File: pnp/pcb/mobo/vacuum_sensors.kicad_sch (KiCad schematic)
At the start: 18 parts, among them J33 I2C_AUX, U2 XGZP6857D, U3 XGZP6857D, U4 PCA9545A

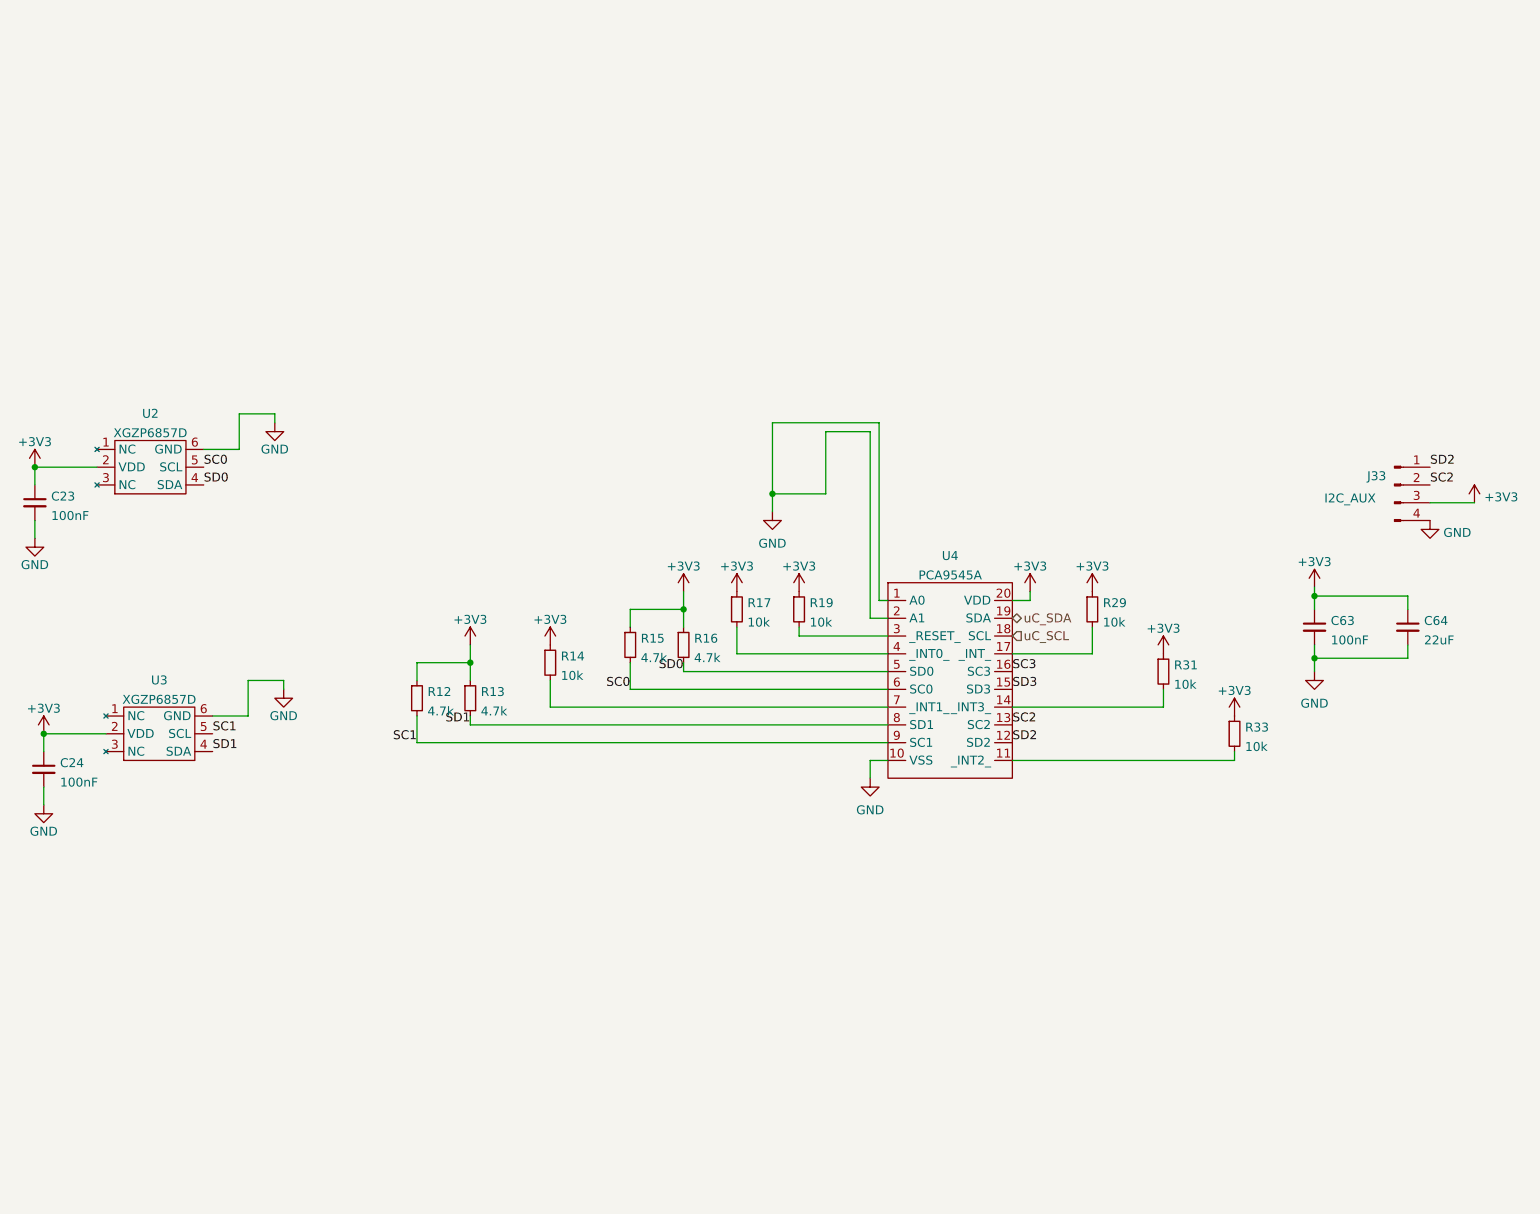
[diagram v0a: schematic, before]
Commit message: Mobo V4A Redesign
Some EMC improvements to schematics.
Reassigned MCU Pins for HW-PWM support.
Changes are still marked with text in the schematics.
Complete PCB Layout reworked
Status: Needs to be verified, and cleaned up a little, but DRC is running green.
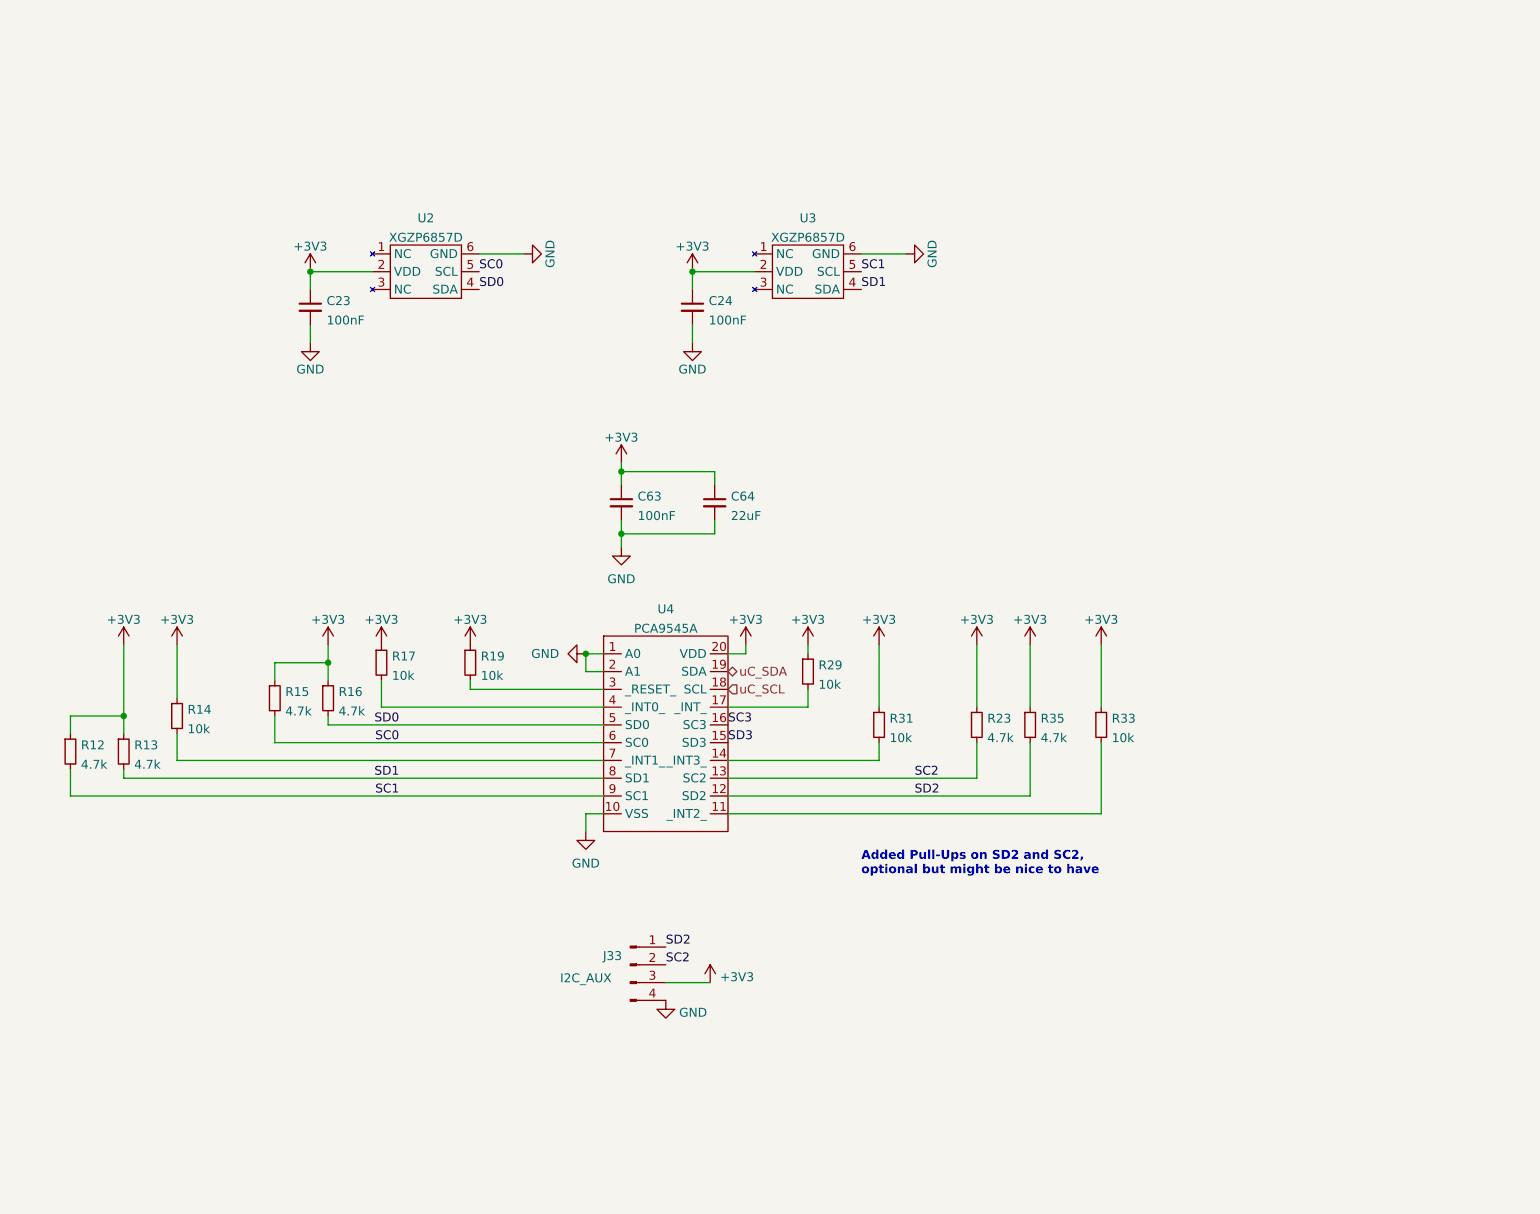
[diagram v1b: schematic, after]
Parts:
- added R23, R35: 4.7k, Resistor_SMD:R_0805_2012Metric, symbol Device:R_Small
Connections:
- net +3V3: now also R23.1, R35.1
- net SC2: now also R23.2
- net SD2: now also R35.2
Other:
- note added: "Added Pull-Ups on SD2 and SC2, optional but might be nice to have"
- moved on the sheet: C23, C24, C63, C64, J33, R12, R13, R14, R15, R16, R17, R19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

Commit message: Redesign finished
Completed Board redesign and adding more EMC improvements.
Changed all the part numbers to have a Mouser orderable design (except the JST connectors)
All outputs generated
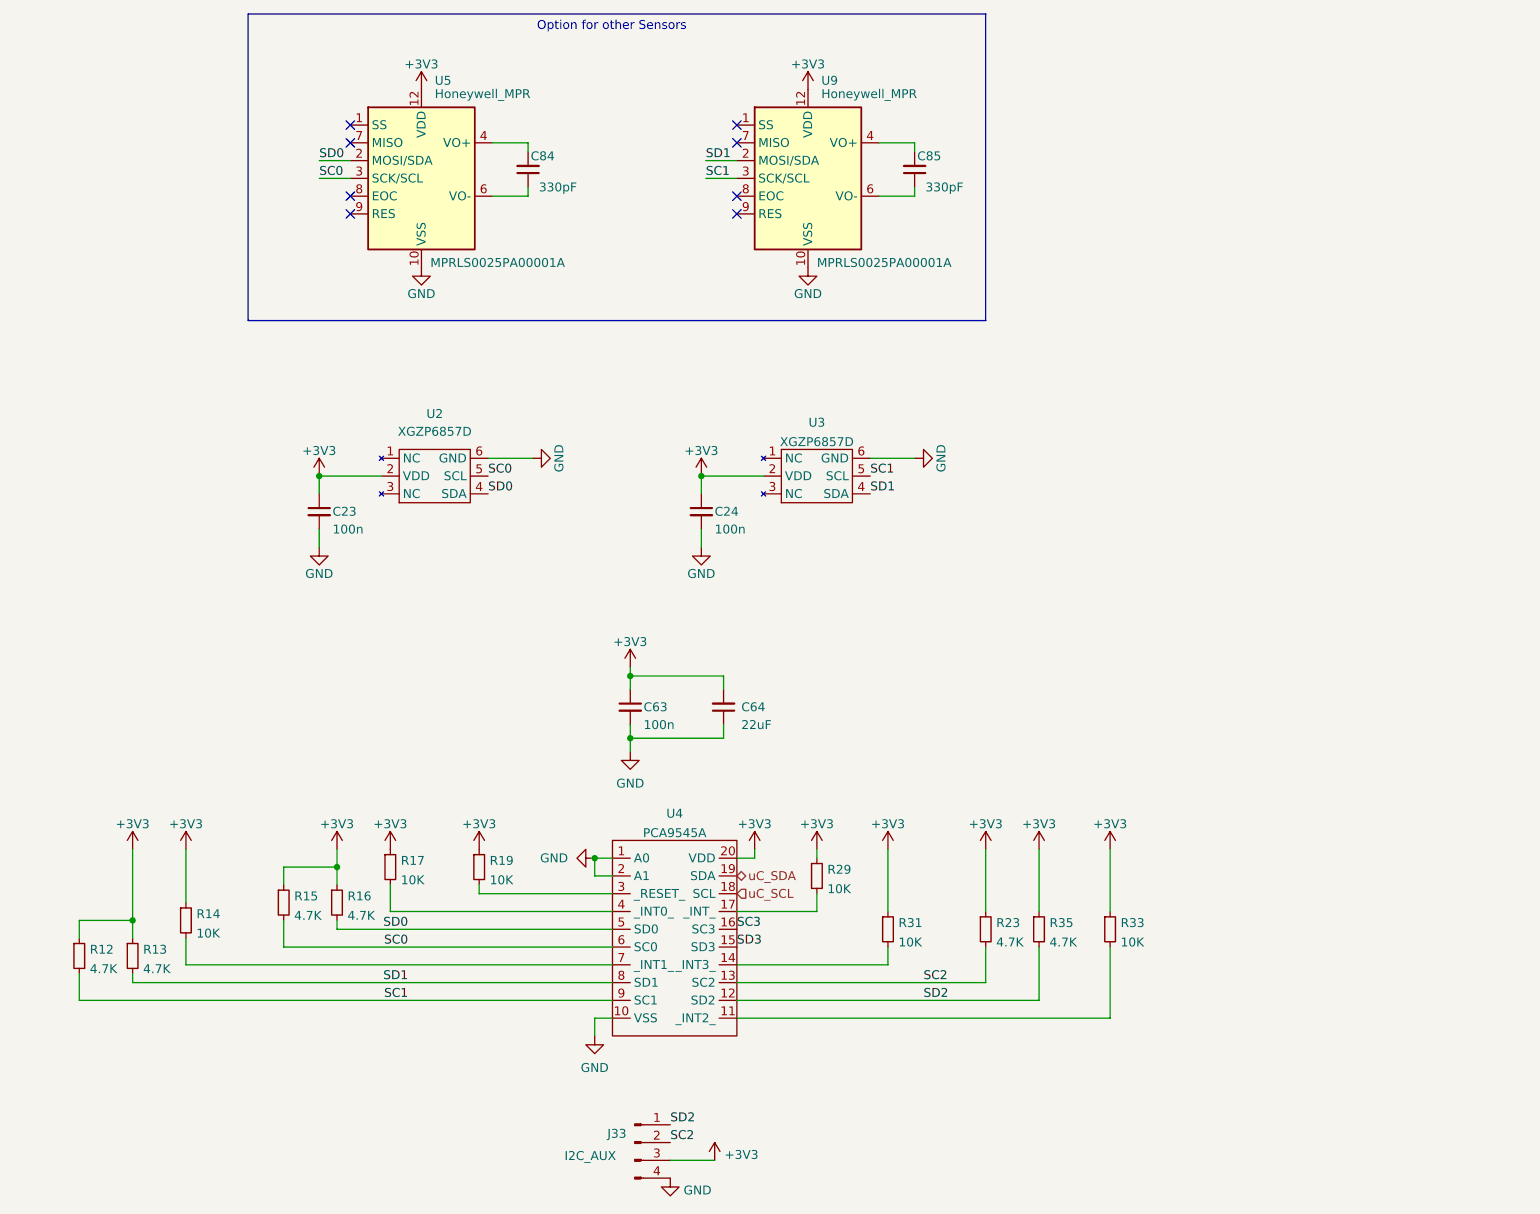
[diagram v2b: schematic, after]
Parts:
- added C84, C85: 330pF, Capacitor_SMD:C_0805_2012Metric, symbol Device:C_Small
- added U5, U9: Honeywell_MPR, Magpie_OpuloLibrary:Honeywell_MPR_5x5mm_LGA12, symbol Magpie_OpuloLibrary:Honeywell_MPR
- C23, C24, C63: value 100nF -> 100n; Mouser (none) -> 710-885012207098
- C64: Mouser (none) -> 81-GRM21BR61E226ME4K
- J33: Mouser (none) -> 571-5-146277-4
- R12, R13, R15, R16, R23, R35: value 4.7k -> 4.7K; Mouser (none) -> 603-RC0805FR-104K7L
- R14, R17, R19, R29, R31, R33: value 10k -> 10K; Mouser (none) -> 603-RC0805FR-1010KL
- U2, U3: Mouser (none) -> -
- U4: Mouser (none) -> 771-PCA9545APW-T
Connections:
- net +3V3: now also C64.2, U5.12 (VDD), U9.12 (VDD); no longer C64.1
- net GND: now also C64.1, U5.10 (VSS), U9.10 (VSS); no longer C64.2
- net SC0: now also U5.3 (SCK/SCL)
- net SC1: now also U9.3 (SCK/SCL)
- net SD0: now also U5.2 (MOSI/SDA)
- net SD1: now also U9.2 (MOSI/SDA)
- new net: C85.1, U9.6 (VO-)
- new net: C85.2, U9.4 (VO+)
- new net: U9.11 (NC), U9.5 (NC)
- new net: U5.11 (NC), U5.5 (NC)
- new net: C84.2, U5.4 (VO+)
- new net: C84.1, U5.6 (VO-)
- no-connect marks 0 -> 8
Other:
- note added: "Option for other Sensors"
- note removed: "Added Pull-Ups on SD2 and SC2, optional but might be nice to have"
- company: Opulo -> Opulo.io
- moved on the sheet: J33, R12, R13, R14, R15, R16, R17, R19, R23, R29, R31, R33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
